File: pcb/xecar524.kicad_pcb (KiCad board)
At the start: 2 copper layers, 62.8 x 89.4 mm, 49 parts, among them J1 JTAG, J2 ICSP, J3 CFG, J4 TEST, U1 MCP1703A-3302_SOT89, U2 Atari_XE_Cartridge_Connector, U3 XC95144XL-TQ100, U4 SST39VF040, U5 PIC24FJ32GA004-I/PT, Y1 32768

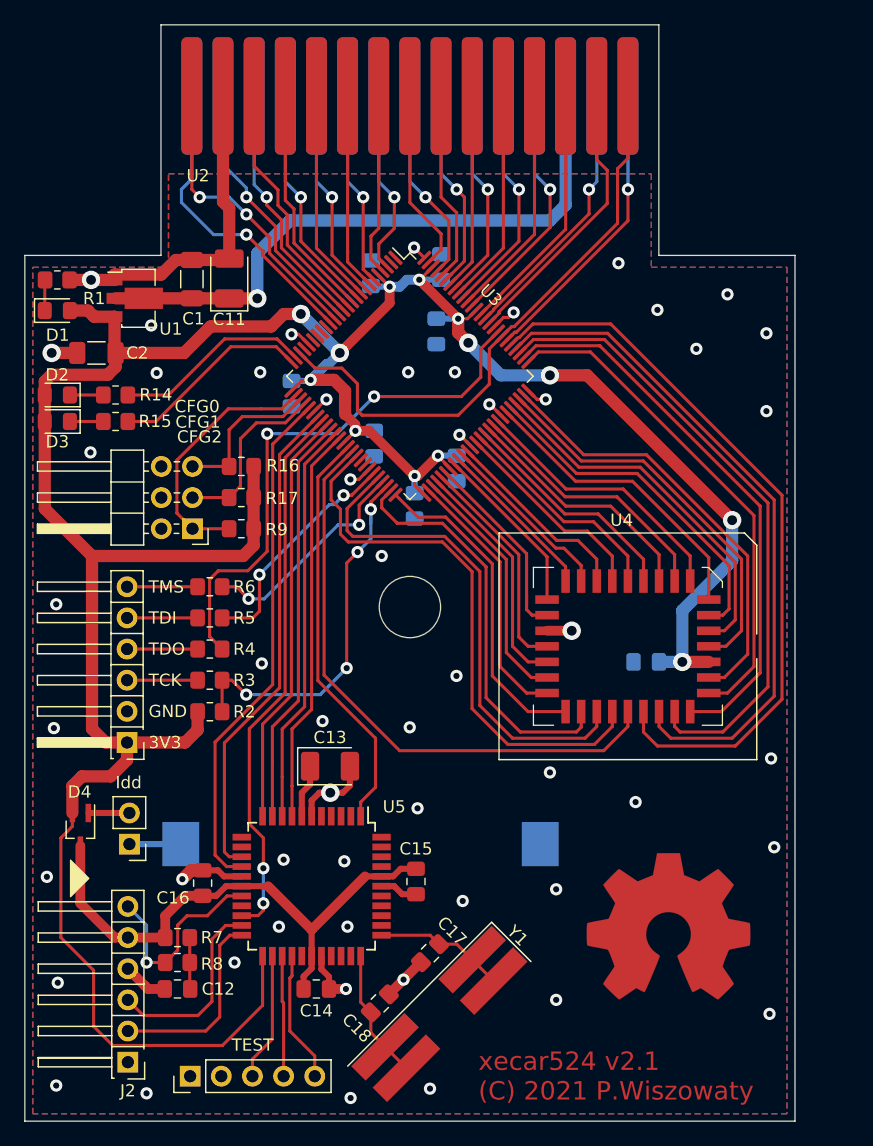
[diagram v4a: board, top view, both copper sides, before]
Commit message: Switch to PIC24FJ64GB004 as RTime8 emulator
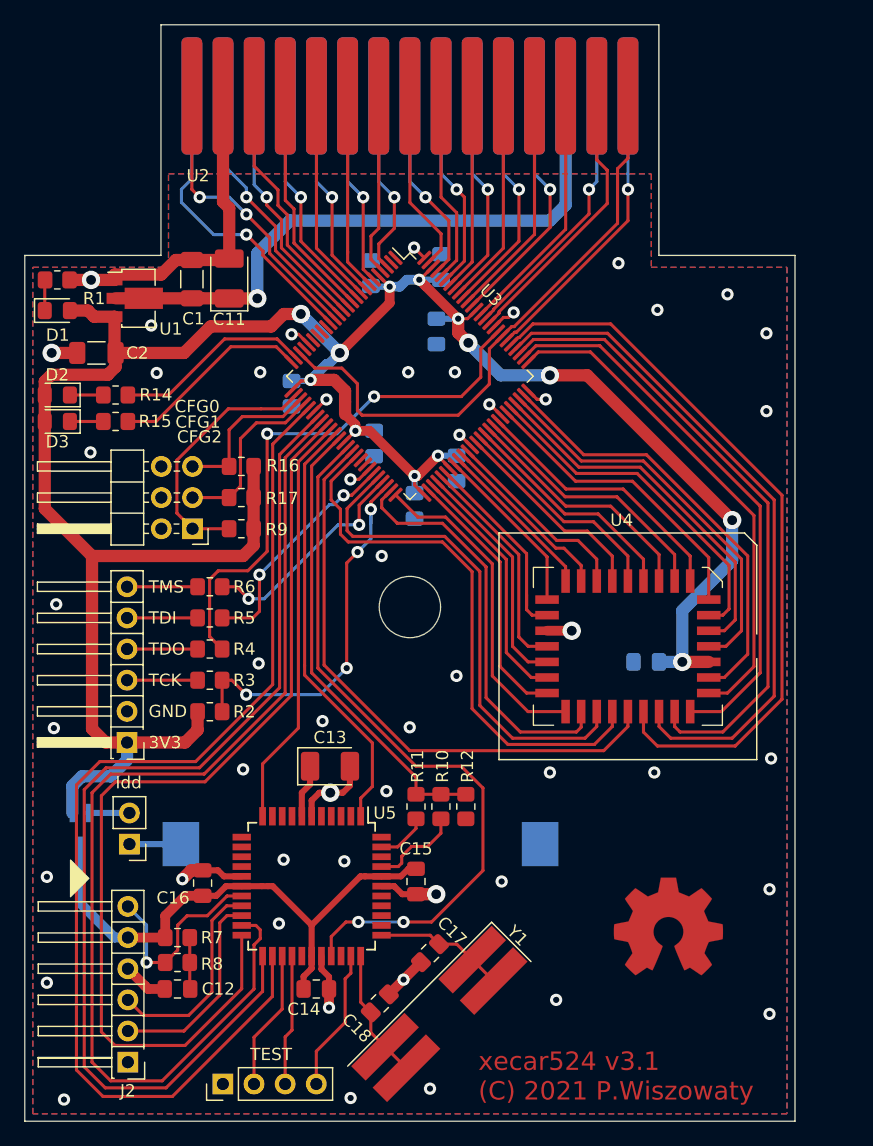
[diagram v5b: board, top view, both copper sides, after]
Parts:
- added R10: 0, Resistor_SMD:R_0805_2012Metric_Pad1.20x1.40mm_HandSolder, F.Cu at (152.5, 108.4)
- added R11: 10k, Resistor_SMD:R_0805_2012Metric_Pad1.20x1.40mm_HandSolder, F.Cu at (150.5, 108.4)
- added R12: 100k, Resistor_SMD:R_0805_2012Metric_Pad1.20x1.40mm_HandSolder, F.Cu at (154.6, 108.4)
- D4: value 1PS70SB15 -> BAT30CWFILM; moved to B.Cu
- J4: footprint Connector_PinHeader_2.54mm:PinHeader_1x05_P2.54mm_Vertical -> Connector_PinHeader_2.54mm:PinHeader_1x04_P2.54mm_Vertical
- LOGO1: footprint Symbol:OSHW-Symbol_13.4x12mm_Copper -> Symbol:OSHW-Symbol_8.9x8mm_Copper
- U5: value PIC24FJ32GA004-I/PT -> PIC24FJxxGB004-IPT
- moved J4 2.74 mm to (134.7, 131.1)
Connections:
- D4 pad 1: Net-(D4-Pad1) -> +3V3
- D4 pad 2: +3V3 -> Net-(D4-Pad2)
- JP1 pad 2: Net-(D4-Pad1) -> Net-(D4-Pad2)
- U3 pad 30: PMCS1 -> PMWR
- U3 pad 32: PMWR -> PMD2
- U3 pad 33: MODE -> PMD0
- U3 pad 34: PMRD -> PMD1
- U3 pad 35: PMD0 -> PMRD
- U3 pad 36: PMD1 -> PMD3
- U3 pad 37: PMD2 -> SENSE3V3
- U3 pad 39: PMD3 -> PMCS1
- U5 pad 10: PMD0 -> Net-(U5-Pad10)
- U5 pad 14: PMWR -> Net-(U5-Pad14)
- U5 pad 15: PMCS1 -> Net-(U5-Pad15)
- U5 pad 19: Net-(U5-Pad19) -> PGD
- U5 pad 20: MODE -> PGC
- U5 pad 21: PGD -> PMD0
- U5 pad 22: PGC -> PMD1
- U5 pad 23: +3V3 -> PMD2
- U5 pad 24: TEST1 -> PMWR
- U5 pad 25: TEST2 -> TEST0
- U5 pad 26: TEST3 -> TEST1
- U5 pad 30: Net-(U5-Pad30) -> PMCS1
- U5 pad 32: Net-(U5-Pad32) -> TEST2
- U5 pad 8: PMD2 -> Net-(U5-Pad8)
- U5 pad 9: PMD1 -> Net-(U5-Pad9)
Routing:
- net PMD0: track 33.5 -> 88.1 mm
- net PMD2: track 32.4 -> 86.7 mm
- net PMWR: track 40.2 -> 89.9 mm
- net PMD1: track 32.9 -> 79.5 mm
- net MODE: track 44.8 -> 0.00 mm, vias 2 -> 0
- net +3V3: track 246.5 -> 207.9 mm
- net SENSE3V3: track 0.00 -> 37.5 mm
- net PMCS1: track 42.2 -> 59.5 mm, vias 0 -> 2
- net TEST0: track 0.00 -> 11.4 mm
- net TEST3: track 10.7 -> 0.00 mm
- net Net-(R10-Pad2): track 0.00 -> 7.46 mm
- net Net-(R11-Pad2): track 0.00 -> 4.22 mm
- net Net-(D4-Pad1): track 3.35 -> 0.00 mm
- net Net-(D4-Pad2): track 0.00 -> 3.35 mm
- net GND: track 71.3 -> 73.1 mm, vias 54 -> 51
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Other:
- board text added: "xecar524 v3.1 (C) 2021 P.Wiszowaty"
- board text removed: "xecar524 v2.1 (C) 2021 P.Wiszowaty"
